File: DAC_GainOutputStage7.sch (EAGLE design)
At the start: 72 parts, among them J1 1935190, J3 SJ-63033A, U1 LM317MQDCYR, U2 LM317MQDCYR

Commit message: Ordered boards
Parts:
- added TP3, TP4: TPB2,54, Dual Mono Amp Library:TPB2,54
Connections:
- net N$18: now also TP3.TP
- net N$3: now also TP4.TP
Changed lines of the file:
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@@
 <part name="VR1" library="Dual Mono Amp Library" library_urn="urn:adsk.eagle:library:47621477" deviceset="PVG5A101C03R00" device="" package3d_urn="urn:adsk.eagle:package:49125174/1"/>
 <part name="VR2" library="Dual Mono Amp Library" library_urn="urn:adsk.eagle:library:47621477" deviceset="PVG5A101C03R00" device="" package3d_urn="urn:adsk.eagle:package:49125174/1"/>
+<part name="TP3" library="Dual Mono Amp Library" library_urn="urn:adsk.eagle:library:47621477" deviceset="TP" device="B2,54" package3d_urn="urn:adsk.eagle:package:27948/1"/>
+<part name="TP4" library="Dual Mono Amp Library" library_urn="urn:adsk.eagle:library:47621477" deviceset="TP" device="B2,54" package3d_urn="urn:adsk.eagle:package:27948/1"/>
 </parts>
 <sheets>
@@
 <attribute name="NAME" x="78.74" y="184.15" size="1.778" layer="95" rot="MR90" align="center-left"/>
 <attribute name="VALUE" x="76.2" y="184.15" size="1.778" layer="96" rot="MR90" align="center-left"/>
+</instance>
+<instance part="TP3" gate="G$1" x="50.8" y="114.3" smashed="yes" rot="R180">
+<attribute name="NAME" x="52.07" y="113.03" size="1.778" layer="95" rot="R180"/>
+<attribute name="TP_SIGNAL_NAME" x="49.53" y="115.57" size="1.778" layer="97" rot="R180"/>
+</instance>
+<instance part="TP4" gate="G$1" x="149.86" y="114.3" smashed="yes" rot="R180">
+<attribute name="NAME" x="151.13" y="113.03" size="1.778" layer="95" rot="R180"/>
+<attribute name="TP_SIGNAL_NAME" x="148.59" y="115.57" size="1.778" layer="97" rot="R180"/>
 </instance>
 </instances>
@@
 <wire x1="20.32" y1="121.92" x2="25.4" y2="121.92" width="0.1524" layer="91"/>
 <junction x="25.4" y="121.92"/>
+<pinref part="TP3" gate="G$1" pin="TP"/>
+<wire x1="50.8" y1="116.84" x2="50.8" y2="121.92" width="0.1524" layer="91"/>
 </segment>
 </net>
@@
 <pinref part="SX2" gate="G$1" pin="8"/>
 <wire x1="180.34" y1="116.84" x2="185.42" y2="116.84" width="0.1524" layer="91"/>
-</segment>
-</net>
+<pinref part="TP4" gate="G$1" pin="TP"/>
+<wire x1="149.86" y1="116.84" x2="149.86" y2="121.92" width="0.1524" layer="91"/>
+</segment>
+</net>

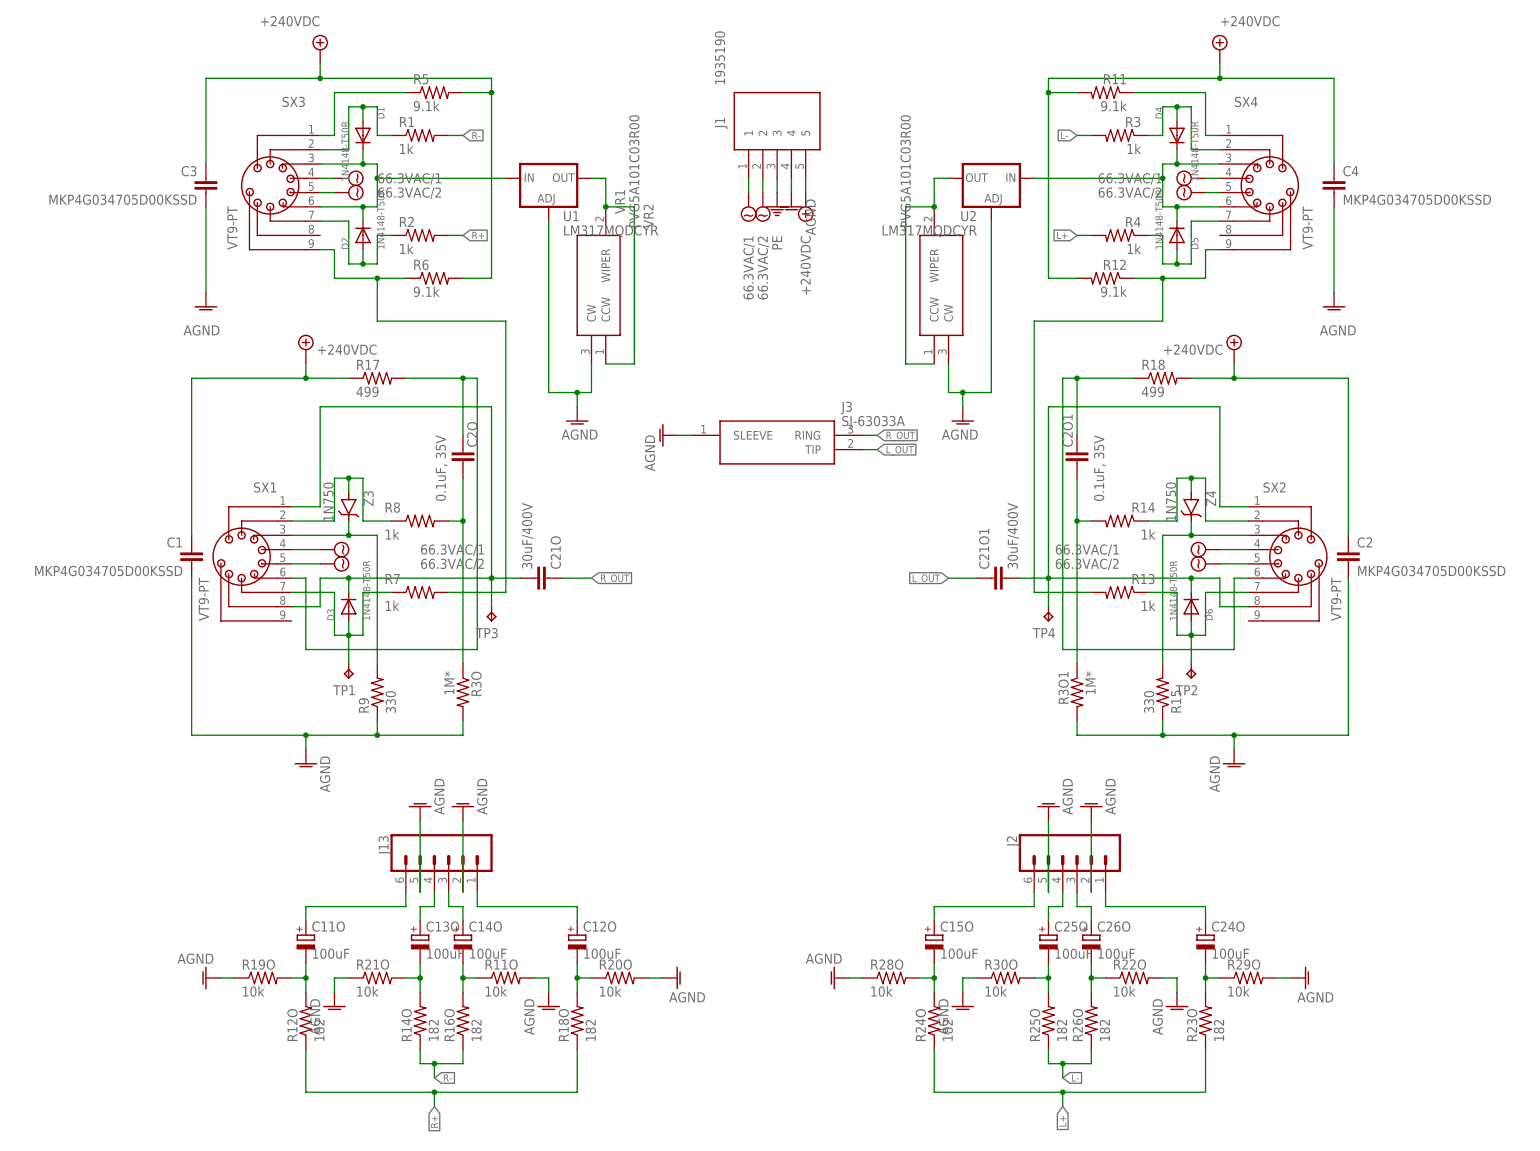
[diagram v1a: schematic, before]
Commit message: Updated PSU and added headphone protection to output stage
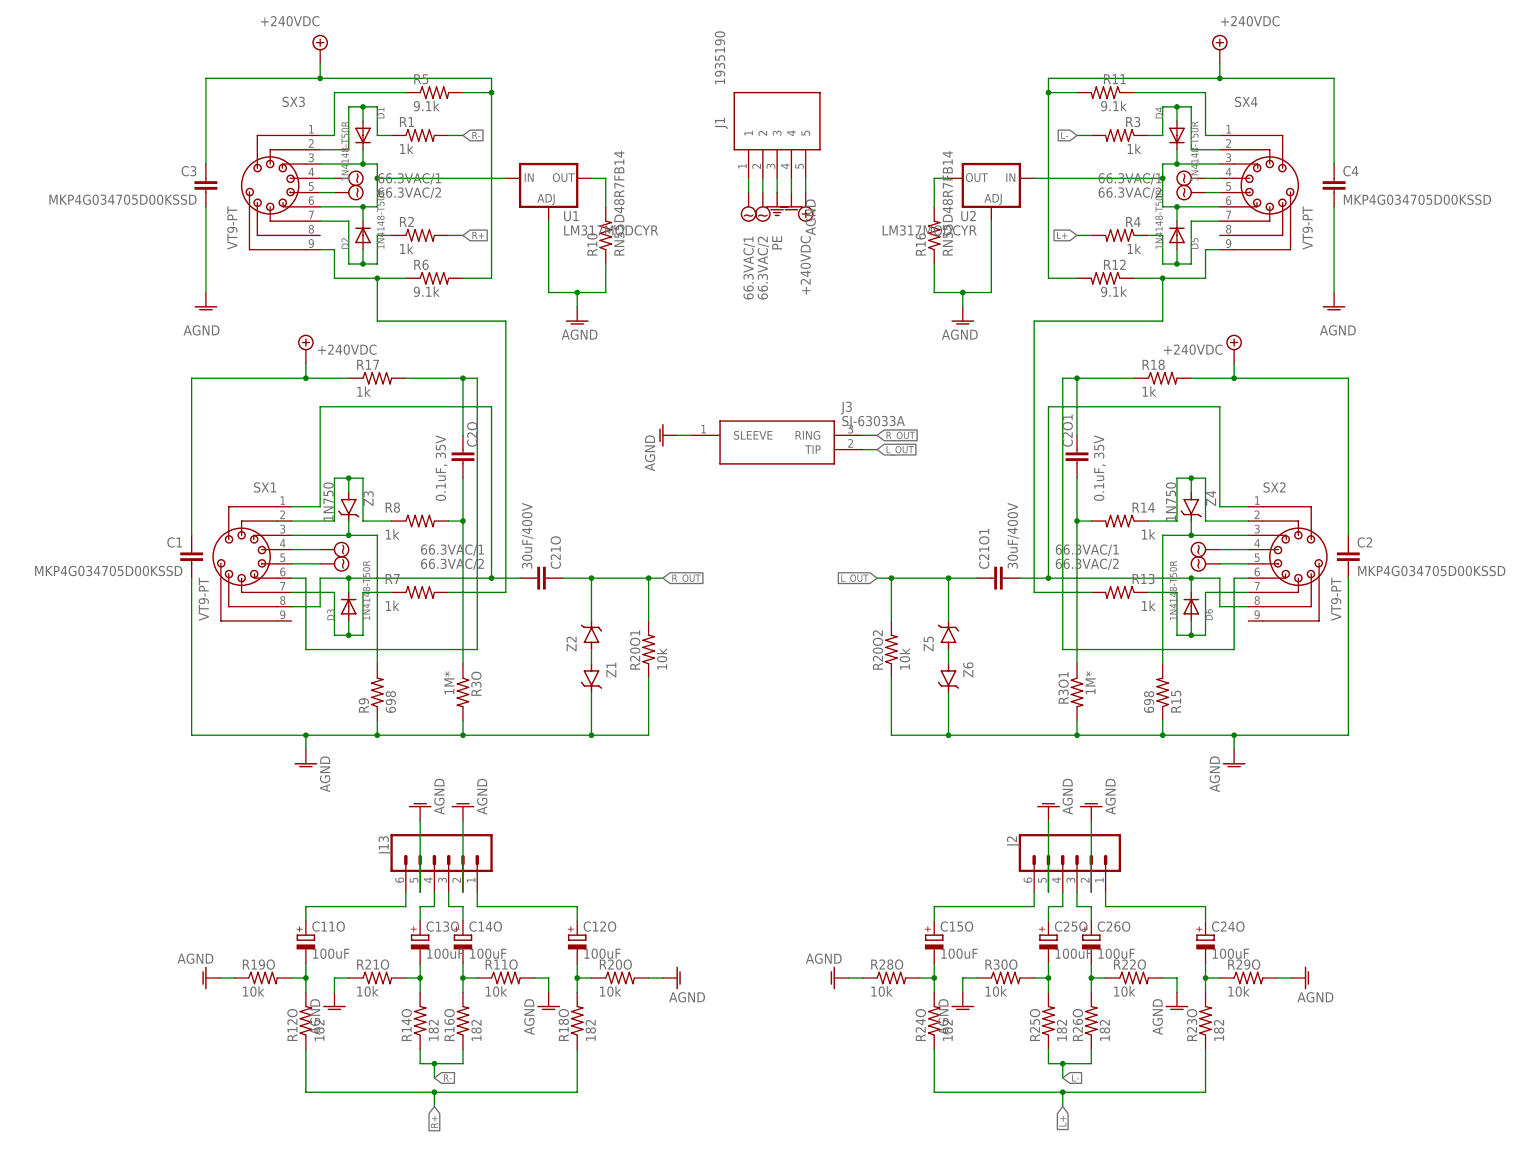
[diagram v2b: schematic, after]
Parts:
- removed TP1, TP2, TP3, TP4: TPB2,54, Dual Mono Amp Library:TPB2,54
- removed VR1, VR2: PVG5A101C03R00, Dual Mono Amp Library:PVG5A101C03R00
- added R10, R16: RN55D48R7FB14, Dual Mono Amp Library:RN55D48R7FB14
- added R20O1, R20O2: 10k, Dual Mono Amp Library:LR1F10K
- added Z1, Z2, Z5, Z6: (no value), Dual Mono Amp Library:BZX79-C16,113
- R15, R9: value 330 -> 698; device Dual Mono Amp Library:LR1F330R -> Dual Mono Amp Library:MF0207FTE52-698R
- R17, R18: value 499 -> 1k; device Dual Mono Amp Library:PR02000204990FA100 -> Dual Mono Amp Library:MFR200FRF52-1K
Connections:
- new net N$41: Z1.A, Z2.A
- new net N$42: Z5.A, Z6.A
- net AGND: now also R10.1, R16.1, R20O1.1, R20O2.1, Z1.C, Z6.C; no longer VR1.CW, VR2.CW
- net L_OUT: now also R20O2.2, Z5.C
- net N$18: no longer TP3.TP
- net N$23: no longer TP1.TP
- net N$29: no longer TP2.TP
- net N$3: no longer TP4.TP
- net N$37: now also R10.2; no longer VR2.CCW, VR2.WIPER
- net N$38: now also R16.2; no longer VR1.CCW, VR1.WIPER
- net R_OUT: now also R20O1.2, Z2.C

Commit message: Preliminary update complete for new tube
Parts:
- added R19, R20: 15k, Dual Mono Amp Library:CPF215K000FKE14
- R10, R16: value RN55D48R7FB14 -> 76.8; device Dual Mono Amp Library:RN55D48R7FB14 -> Dual Mono Amp Library:RN55D76R8FB14
- R11, R5: value 9.1k -> 18k; device Dual Mono Amp Library:PR02000209101FA100 -> Dual Mono Amp Library:PR02000201802FA100
- R12, R6: value 9.1k -> 3k; device Dual Mono Amp Library:PR02000209101FA100 -> Dual Mono Amp Library:PR02000203001FA100
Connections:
- new net N$43: R6.1, SX3.9
- new net N$44: R12.1, SX4.9
- net +240VDC: now also R19.2, R20.1; no longer R12.2, R6.2
- net N$1: now also R19.1, R6.2; no longer R6.1, SX3.9
- net N$9: now also R12.2, R20.2; no longer R12.1, SX4.9
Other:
- moved on the sheet: R12, R6

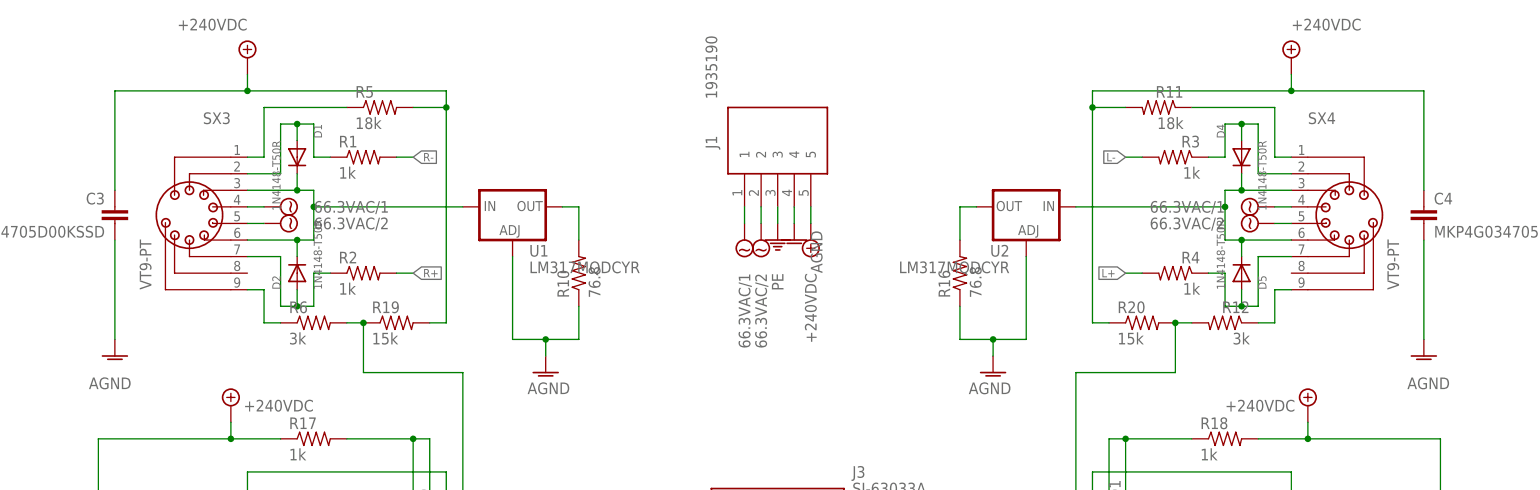
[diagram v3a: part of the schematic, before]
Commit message: Added new spice model and work on output stage
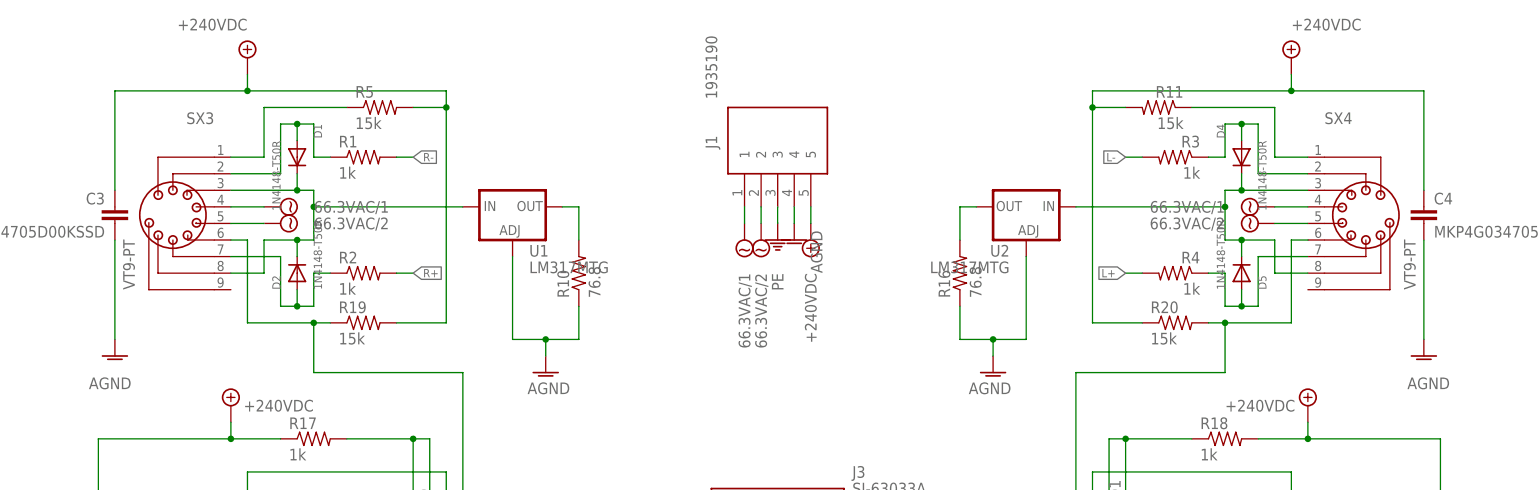
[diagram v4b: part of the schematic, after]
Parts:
- removed R12, R6: 3k, Dual Mono Amp Library:PR02000203001FA100
- R10, R16: device Dual Mono Amp Library:RN55D76R8FB14 -> Dual Mono Amp Library:YR1B76R8CC
- R11, R5: value 18k -> 15k; device Dual Mono Amp Library:PR02000201802FA100 -> Dual Mono Amp Library:CPF215K000FKE14
- U1, U2: value LM317MQDCYR -> LM317MTG; device Dual Mono Amp Library:LM317MQDCYR -> Dual Mono Amp Library:LM317MTG
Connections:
- removed net N$43: R6.1, SX3.9
- removed net N$44: R12.1, SX4.9
- net N$1: now also SX3.6; no longer R6.2
- net N$22: now also SX3.8; no longer SX3.6
- net N$7: now also SX4.8; no longer SX4.6
- net N$9: now also SX4.6; no longer R12.2
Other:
- moved on the sheet: R19, R20, SX3, SX4

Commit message: Finished boards and spice models
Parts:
- R15, R9: value 698 -> 249; device Dual Mono Amp Library:MF0207FTE52-698R -> Dual Mono Amp Library:MBB02070C2490FRP00
- R17, R18: value 1k -> 402; device Dual Mono Amp Library:MFR200FRF52-1K -> Dual Mono Amp Library:RWR80S4020FRB12
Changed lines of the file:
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@@
 <part name="R7" library="Dual Mono Amp Library" library_urn="urn:adsk.eagle:library:47621477" deviceset="LR1F1K0" device="" package3d_urn="urn:adsk.eagle:package:23491/2" value="1k"/>
 <part name="R8" library="Dual Mono Amp Library" library_urn="urn:adsk.eagle:library:47621477" deviceset="LR1F1K0" device="" package3d_urn="urn:adsk.eagle:package:23491/2" value="1k"/>
-<part name="R9" library="Dual Mono Amp Library" library_urn="urn:adsk.eagle:library:47621477" deviceset="MF0207FTE52-698R" device="" package3d_urn="urn:adsk.eagle:package:23491/2" value="698"/>
+<part name="R9" library="Dual Mono Amp Library" library_urn="urn:adsk.eagle:library:47621477" deviceset="MBB02070C2490FRP00" device="" package3d_urn="urn:adsk.eagle:package:23491/2" value="249"/>
 <part name="D1" library="Dual Mono Amp Library" library_urn="urn:adsk.eagle:library:47621477" deviceset="1N4148-T50R" device="" package3d_urn="urn:adsk.eagle:package:48500905/1"/>
 <part name="D2" library="Dual Mono Amp Library" library_urn="urn:adsk.eagle:library:47621477" deviceset="1N4148-T50R" device="" package3d_urn="urn:adsk.eagle:package:48500905/1"/>
@@
 <part name="R13" library="Dual Mono Amp Library" library_urn="urn:adsk.eagle:library:47621477" deviceset="LR1F1K0" device="" package3d_urn="urn:adsk.eagle:package:23491/2" value="1k"/>
 <part name="R14" library="Dual Mono Amp Library" library_urn="urn:adsk.eagle:library:47621477" deviceset="LR1F1K0" device="" package3d_urn="urn:adsk.eagle:package:23491/2" value="1k"/>
-<part name="R15" library="Dual Mono Amp Library" library_urn="urn:adsk.eagle:library:47621477" deviceset="MF0207FTE52-698R" device="" package3d_urn="urn:adsk.eagle:package:23491/2" value="698"/>
+<part name="R15" library="Dual Mono Amp Library" library_urn="urn:adsk.eagle:library:47621477" deviceset="MBB02070C2490FRP00" device="" package3d_urn="urn:adsk.eagle:package:23491/2" value="249"/>
 <part name="D4" library="Dual Mono Amp Library" library_urn="urn:adsk.eagle:library:47621477" deviceset="1N4148-T50R" device="" package3d_urn="urn:adsk.eagle:package:48500905/1"/>
 <part name="D5" library="Dual Mono Amp Library" library_urn="urn:adsk.eagle:library:47621477" deviceset="1N4148-T50R" device="" package3d_urn="urn:adsk.eagle:package:48500905/1"/>
@@
 <part name="Z3" library="Dual Mono Amp Library" library_urn="urn:adsk.eagle:library:47621477" deviceset="1N750" device="" package3d_urn="urn:adsk.eagle:package:48500160/1"/>
 <part name="Z4" library="Dual Mono Amp Library" library_urn="urn:adsk.eagle:library:47621477" deviceset="1N750" device="" package3d_urn="urn:adsk.eagle:package:48500160/1"/>
-<part name="R17" library="Dual Mono Amp Library" library_urn="urn:adsk.eagle:library:47621477" deviceset="MFR200FRF52-1K" device="" package3d_urn="urn:adsk.eagle:package:23577/1" value="1k"/>
-<part name="R18" library="Dual Mono Amp Library" library_urn="urn:adsk.eagle:library:47621477" deviceset="MFR200FRF52-1K" device="" package3d_urn="urn:adsk.eagle:package:23577/1" value="1k"/>
+<part name="R17" library="Dual Mono Amp Library" library_urn="urn:adsk.eagle:library:47621477" deviceset="RWR80S4020FRB12" device="" package3d_urn="urn:adsk.eagle:package:23577/1" value="402"/>
+<part name="R18" library="Dual Mono Amp Library" library_urn="urn:adsk.eagle:library:47621477" deviceset="RWR80S4020FRB12" device="" package3d_urn="urn:adsk.eagle:package:23577/1" value="402"/>
 <part name="R10" library="Dual Mono Amp Library" library_urn="urn:adsk.eagle:library:47621477" deviceset="YR1B76R8CC" device="" package3d_urn="urn:adsk.eagle:package:23491/2" value="76.8"/>
 <part name="R16" library="Dual Mono Amp Library" library_urn="urn:adsk.eagle:library:47621477" deviceset="YR1B76R8CC" device="" package3d_urn="urn:adsk.eagle:package:23491/2" value="76.8"/>
